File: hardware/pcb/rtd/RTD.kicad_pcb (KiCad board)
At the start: 2 copper layers, 44 x 29 mm, 22 parts, among them J1 JACK_TRS_3PINS, U1 OPA2340, U2 OPA2340

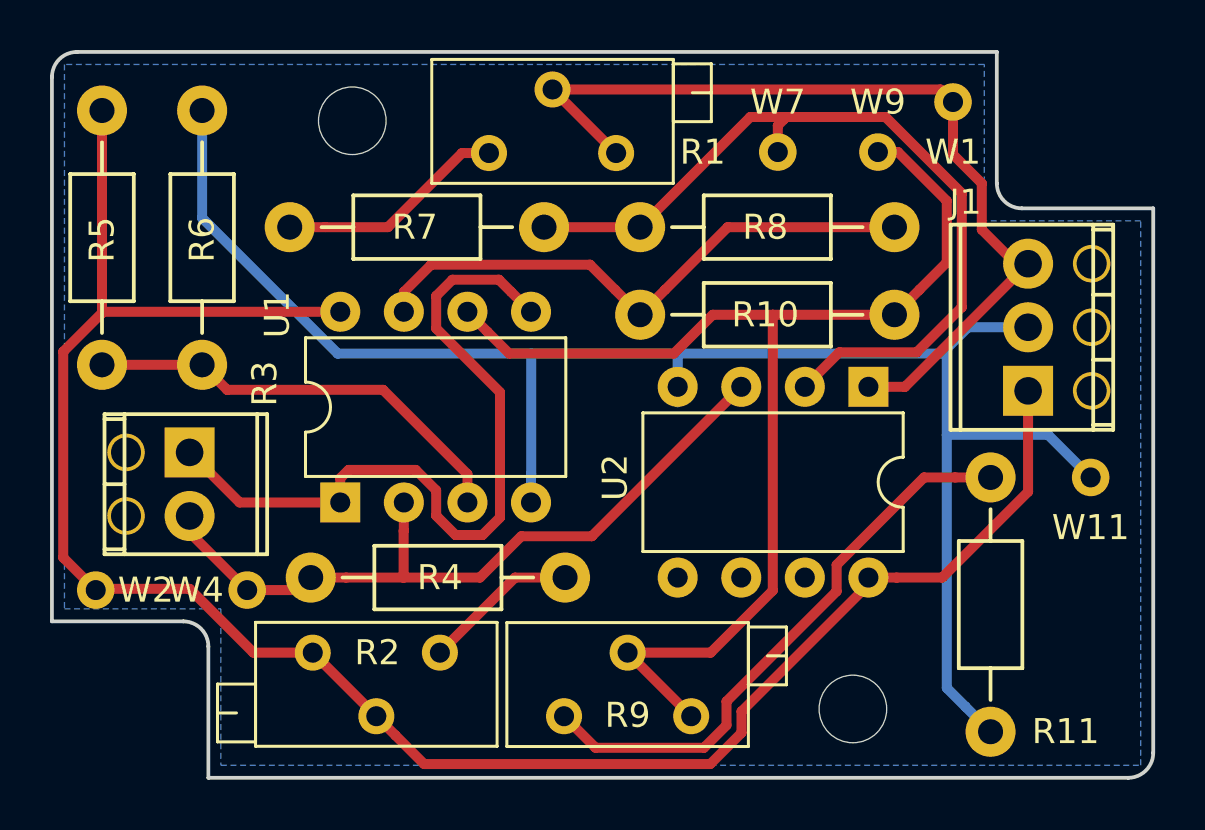
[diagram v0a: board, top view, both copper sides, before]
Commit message: feat: General PCB improvements
redo Scheme

Issue #14
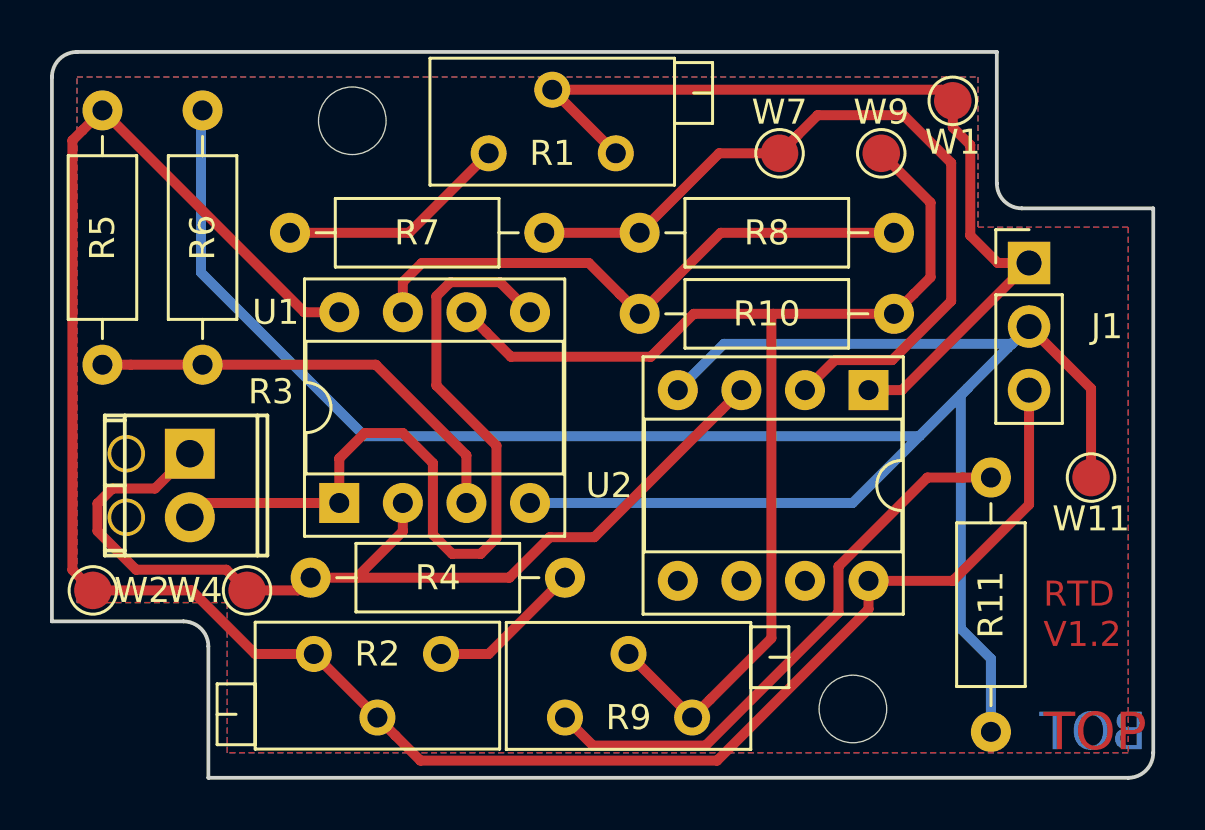
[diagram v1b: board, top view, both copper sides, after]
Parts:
- J1: value JACK_TRS_3PINS -> Conn_01x03; footprint Pheonix:TerminalBlock_Pheonix_MPT-2.54mm_3pol -> Connector_PinHeader_2.54mm:PinHeader_1x03_P2.54mm_Vertical
- R1, R2, R9: footprint Potentiometers:Potentiometer_Trimmer_Bourns_3296Z -> Potentiometer_THT:Potentiometer_Bourns_3296Z_Horizontal
- R10, R11, R4, R5, R6, R7, R8: footprint ThroughHole:Resistor_Horizontal_RM10mm -> Resistor_THT:R_Axial_DIN0207_L6.3mm_D2.5mm_P10.16mm_Horizontal
- R3: value THERMISTOR -> PT100
- U1, U2: footprint Housings_DIP:DIP-8_W7.62mm -> Package_DIP:DIP-8_W7.62mm_Socket
- W1: value TEST_1P -> ~; footprint Measurement_Points:Measurement_Point_Round-TH_Small -> TestPoint:TestPoint_Pad_D1.5mm
- W11: value TEST_11P -> ~; footprint Measurement_Points:Measurement_Point_Round-TH_Small -> TestPoint:TestPoint_Pad_D1.5mm
- W2: value TEST_2P -> ~; footprint Measurement_Points:Measurement_Point_Round-TH_Small -> TestPoint:TestPoint_Pad_D1.5mm
- W4: value TEST_4P -> ~; footprint Measurement_Points:Measurement_Point_Round-TH_Small -> TestPoint:TestPoint_Pad_D1.5mm
- W7: value TEST_7P -> ~; footprint Measurement_Points:Measurement_Point_Round-TH_Small -> TestPoint:TestPoint_Pad_D1.5mm
- W9: value TEST_9P -> ~; footprint Measurement_Points:Measurement_Point_Round-TH_Small -> TestPoint:TestPoint_Pad_D1.5mm
- moved R5 10.2 mm to (17.0, 17.3), turned to 270 degrees
- moved R4 10.2 mm to (35.5, 36.0), turned to 180 degrees
- moved R11 10.2 mm to (52.5, 32.0), turned to 270 degrees
- moved J1 5.11 mm to (54.0, 23.4), turned to 0 degrees
- moved R8 0.23 mm to (48.6, 22.2)
- moved R7 0.23 mm to (34.7, 22.2)
- moved W9 0.14 mm to (48.1, 19.1)
- moved U2 0.13 mm to (47.6, 28.5)
- moved W2 0.11 mm to (16.6, 36.5)
- moved W7 0.09 mm to (44.1, 19.1)
- moved R2 0.07 mm to (30.5, 39.1)
- moved R9 0.06 mm to (35.5, 41.6)
- moved R3 0.05 mm to (20.5, 31.1)
- turned W1 to 180 degrees
- turned W11 to 180 degrees
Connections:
- J1 pad 1: +5V -> /SIGNAL
- J1 pad 2: AGND -> GND
- J1 pad 3: /SIGNAL_T1 -> +5V
- R1 pad 2: /SIGNAL_T1 -> /SIGNAL
- R1 pad 3: /SIGNAL_T1 -> /SIGNAL
- R11 pad 1: AGND -> Net-(R11-Pad1)
- R11 pad 2: Net-(R11-Pad2) -> GND
- R4 pad 1: Net-(R3-Pad2) -> Net-(R2-Pad1)
- R4 pad 2: Net-(R2-Pad1) -> Net-(R3-Pad1)
- R5 pad 1: Net-(R5-Pad1) -> +5V
- R5 pad 2: +5V -> Net-(R5-Pad2)
- R6 pad 1: AGND -> GND
- R6 pad 2: Net-(R5-Pad1) -> Net-(R5-Pad2)
- R9 pad 1: Net-(R11-Pad2) -> Net-(R11-Pad1)
- U1 pad 1: Net-(R3-Pad1) -> Net-(R3-Pad2)
- U1 pad 2: Net-(R3-Pad2) -> Net-(R3-Pad1)
- U1 pad 3: Net-(R5-Pad1) -> Net-(R5-Pad2)
- U1 pad 4: AGND -> GND
- U1 pad 5: Net-(R3-Pad1) -> Net-(R3-Pad2)
- U2 pad 1: /SIGNAL_T1 -> /SIGNAL
- U2 pad 3: Net-(R3-Pad2) -> Net-(R3-Pad1)
- U2 pad 4: AGND -> GND
- U2 pad 5: (no net) -> Net-(U2-Pad5)
- U2 pad 6: (no net) -> Net-(U2-Pad6)
- U2 pad 7: (no net) -> Net-(U2-Pad7)
- W1 pad 1: /SIGNAL_T1 -> /SIGNAL
- W11 pad 1: AGND -> GND
- W4 pad 1: Net-(R3-Pad2) -> Net-(R3-Pad1)
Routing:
- net GND: track 0.00 -> 103.5 mm
- net AGND: track 71.5 -> 0.00 mm, vias 1 -> 0
- net /SIGNAL_T1: track 37.0 -> 0.00 mm
- net /SIGNAL: track 0.00 -> 36.8 mm
- net Net-(R11-Pad2): track 23.2 -> 0.00 mm
- net Net-(R11-Pad1): track 0.00 -> 23.0 mm
- net Net-(R5-Pad2): track 0.00 -> 17.9 mm
- net Net-(R5-Pad1): track 17.5 -> 0.00 mm
- net Net-(R3-Pad1): track 30.8 -> 39.4 mm
- net +5V: track 79.3 -> 82.5 mm
- net Net-(R3-Pad2): track 30.7 -> 33.7 mm
- net Net-(R7-Pad1): track 33.8 -> 31.8 mm
- net Net-(R10-Pad1): track 49.1 -> 47.4 mm
- added copper zone on F.Cu, net +5V
- added copper zone on B.Cu, net GND
- removed copper zone on B.Cu, net AGND
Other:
- board text added: "BOT"
- board text added: "RTD V1.2"
- board text added: "TOP"
